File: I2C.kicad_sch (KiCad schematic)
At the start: 10 parts, among them J601 XH-4A connector, J602 2350514-8, U601 TLA2528IRTER

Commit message: update schematique
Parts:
- renumbered C601 to C26, C602 to C27, C603 to C28, J601 to J13, J602 to J14, R606 to R37, R607 to R38, R601 to R39, R602 to R40, U601 to U11
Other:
- title: 5V Logic I2C -> I2C
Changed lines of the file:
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@@
 	(paper "USLetter")
 	(title_block
-		(title "5V Logic I2C")
+		(title "I2C")
 		(comment 1 "Gérémy Sauvageau")
 	)
@@
 		(on_board yes)
 		(dnp no)
-		(property "Reference" "#PWR0615"
+		(property "Reference" "#PWR089"
 			(at 82.55 130.048 0)
 			(effects
@@
 			(project "SACE-HW"
 				(path "/4c1e5ca8-aa0f-4a8e-bffe-6765adb2e3e8/89fdb234-fe30-4f1f-ac7b-866137add73a"
-					(reference "#PWR0615")
+					(reference "#PWR089")
 					(unit 1)
 				)
@@
 		(dnp no)
 		(fields_autoplaced yes)
-		(property "Reference" "#PWR0605"
+		(property "Reference" "#PWR086"
 			(at 78.74 46.99 0)
 			(effects
@@
 			(project "SACE-HW"
 				(path "/4c1e5ca8-aa0f-4a8e-bffe-6765adb2e3e8/89fdb234-fe30-4f1f-ac7b-866137add73a"
-					(reference "#PWR0605")
+					(reference "#PWR086")
 					(unit 1)
 				)
@@
 		(dnp no)
 		(fields_autoplaced yes)
-		(property "Reference" "#PWR0601"
+		(property "Reference" "#PWR090"
 			(at 110.49 45.72 0)
 			(effects
@@
 			(project "SACE-HW"
 				(path "/4c1e5ca8-aa0f-4a8e-bffe-6765adb2e3e8/89fdb234-fe30-4f1f-ac7b-866137add73a"
-					(reference "#PWR0601")
+					(reference "#PWR090")
 					(unit 1)
 				)
@@
 		(dnp no)
 		(fields_autoplaced yes)
-		(property "Reference" "#PWR0603"
+		(property "Reference" "#PWR082"
 			(at 41.91 46.99 0)
 			(effects
@@
 			(project "SACE-HW"
 				(path "/4c1e5ca8-aa0f-4a8e-bffe-6765adb2e3e8/89fdb234-fe30-4f1f-ac7b-866137add73a"
-					(reference "#PWR0603")
+					(reference "#PWR082")
 					(unit 1)
 				)
@@
 		(on_board yes)
 		(dnp no)
-		(property "Reference" "#PWR0607"
+		(property "Reference" "#PWR087"
 			(at 78.74 58.928 0)
 			(effects
@@
 			(project "SACE-HW"
 				(path "/4c1e5ca8-aa0f-4a8e-bffe-6765adb2e3e8/89fdb234-fe30-4f1f-ac7b-866137add73a"
-					(reference "#PWR0607")
+					(reference "#PWR087")
 					(unit 1)
 				)
@@
 		(on_board yes)
 		(dnp no)
-		(property "Reference" "#PWR0606"
+		(property "Reference" "#PWR083"
 			(at 46.99 57.658 0)
 			(effects
@@
 			(project "SACE-HW"
 				(path "/4c1e5ca8-aa0f-4a8e-bffe-6765adb2e3e8/89fdb234-fe30-4f1f-ac7b-866137add73a"
-					(reference "#PWR0606")
+					(reference "#PWR083")
 					(unit 1)
 				)
@@
 		(on_board yes)
 		(dnp no)
-		(property "Reference" "U601"
+		(property "Reference" "U11"
 			(at 102.87 74.93 0)
 			(effects
@@
 			(project "SACE-HW"
 				(path "/4c1e5ca8-aa0f-4a8e-bffe-6765adb2e3e8/89fdb234-fe30-4f1f-ac7b-866137add73a"
-					(reference "U601")
+					(reference "U11")
 					(unit 1)
 				)
@@
 		(dnp no)
 		(fields_autoplaced yes)
-		(property "Reference" "#PWR0608"
+		(property "Reference" "#PWR088"
 			(at 81.28 86.36 0)
 			(effects
@@
 			(project "SACE-HW"
 				(path "/4c1e5ca8-aa0f-4a8e-bffe-6765adb2e3e8/89fdb234-fe30-4f1f-ac7b-866137add73a"
-					(reference "#PWR0608")
+					(reference "#PWR088")
 					(unit 1)
 				)
@@
 		(dnp no)
 		(fields_autoplaced yes)
-		(property "Reference" "R601"
+		(property "Reference" "R39"
 			(at 107.95 46.9899 90)
 			(effects
@@
 			(project "SACE-HW"
 				(path "/4c1e5ca8-aa0f-4a8e-bffe-6765adb2e3e8/89fdb234-fe30-4f1f-ac7b-866137add73a"
-					(reference "R601")
+					(reference "R39")
 					(unit 1)
 				)
@@
 		(on_board yes)
 		(dnp no)
-		(property "Reference" "#PWR0613"
+		(property "Reference" "#PWR085"
 			(at 69.85 118.618 0)
 			(effects
@@
 			(project "SACE-HW"
 				(path "/4c1e5ca8-aa0f-4a8e-bffe-6765adb2e3e8/89fdb234-fe30-4f1f-ac7b-866137add73a"
-					(reference "#PWR0613")
+					(reference "#PWR085")
 					(unit 1)
 				)
@@
 		(dnp no)
 		(fields_autoplaced yes)
-		(property "Reference" "#PWR0604"
+		(property "Reference" "#PWR084"
 			(at 52.07 46.99 0)
 			(effects
@@
 			(project "SACE-HW"
 				(path "/4c1e5ca8-aa0f-4a8e-bffe-6765adb2e3e8/89fdb234-fe30-4f1f-ac7b-866137add73a"
-					(reference "#PWR0604")
+					(reference "#PWR084")
 					(unit 1)
 				)
@@
 		(dnp no)
 		(fields_autoplaced yes)
-		(property "Reference" "J602"
+		(property "Reference" "J14"
 			(at 147.32 110.4899 0)
 			(effects
@@
 			(project "SACE-HW"
 				(path "/4c1e5ca8-aa0f-4a8e-bffe-6765adb2e3e8/89fdb234-fe30-4f1f-ac7b-866137add73a"
-					(reference "J602")
+					(reference "J14")
 					(unit 1)
 				)
@@
 		(dnp no)
 		(fields_autoplaced yes)
-		(property "Reference" "J601"
+		(property "Reference" "J13"
 			(at 71.755 40.64 0)
 			(effects
@@
 			(project "SACE-HW"
 				(path "/4c1e5ca8-aa0f-4a8e-bffe-6765adb2e3e8/89fdb234-fe30-4f1f-ac7b-866137add73a"
-					(reference "J601")
+					(reference "J13")
 					(unit 1)
 				)
@@
 		(dnp no)
 		(fields_autoplaced yes)
-		(property "Reference" "R602"
+		(property "Reference" "R40"
 			(at 118.11 46.9899 90)
 			(effects
@@
 			(project "SACE-HW"
 				(path "/4c1e5ca8-aa0f-4a8e-bffe-6765adb2e3e8/89fdb234-fe30-4f1f-ac7b-866137add73a"
-					(reference "R602")
+					(reference "R40")
 					(unit 1)
 				)
@@
 		(on_board yes)
 		(dnp no)
-		(property "Reference" "C602"
+		(property "Reference" "C27"
 			(at 52.07 44.45 90)
 			(effects
@@
 			(project "SACE-HW"
 				(path "/4c1e5ca8-aa0f-4a8e-bffe-6765adb2e3e8/89fdb234-fe30-4f1f-ac7b-866137add73a"
-					(reference "C602")
+					(reference "C27")
 					(unit 1)
 				)
@@
 		(on_board yes)
 		(dnp no)
-		(property "Reference" "C601"
+		(property "Reference" "C26"
 			(at 41.91 44.45 90)
 			(effects
@@
 			(project "SACE-HW"
 				(path "/4c1e5ca8-aa0f-4a8e-bffe-6765adb2e3e8/89fdb234-fe30-4f1f-ac7b-866137add73a"
-					(reference "C601")
+					(reference "C26")
 					(unit 1)
 				)
@@
 		(on_board yes)
 		(dnp no)
-		(property "Reference" "R606"
+		(property "Reference" "R37"
 			(at 68.58 95.25 90)
 			(effects
@@
 			(project "SACE-HW"
 				(path "/4c1e5ca8-aa0f-4a8e-bffe-6765adb2e3e8/89fdb234-fe30-4f1f-ac7b-866137add73a"
-					(reference "R606")
+					(reference "R37")
 					(unit 1)
 				)
@@
 		(on_board yes)
 		(dnp yes)
-		(property "Reference" "R607"
+		(property "Reference" "R38"
 			(at 68.58 105.41 90)
 			(effects
@@
 			(project "SACE-HW"
 				(path "/4c1e5ca8-aa0f-4a8e-bffe-6765adb2e3e8/89fdb234-fe30-4f1f-ac7b-866137add73a"
-					(reference "R607")
+					(reference "R38")
 					(unit 1)
 				)
@@
 		(on_board yes)
 		(dnp no)
-		(property "Reference" "#PWR0610"
+		(property "Reference" "#PWR091"
 			(at 123.19 89.408 0)
 			(effects
@@
 			(project "SACE-HW"
 				(path "/4c1e5ca8-aa0f-4a8e-bffe-6765adb2e3e8/89fdb234-fe30-4f1f-ac7b-866137add73a"
-					(reference "#PWR0610")
+					(reference "#PWR091")
 					(unit 1)
 				)
@@
 		(on_board yes)
 		(dnp no)
-		(property "Reference" "C603"
+		(property "Reference" "C28"
 			(at 81.28 120.65 90)
 			(effects
@@
 			(project "SACE-HW"
 				(path "/4c1e5ca8-aa0f-4a8e-bffe-6765adb2e3e8/89fdb234-fe30-4f1f-ac7b-866137add73a"
-					(reference "C603")
+					(reference "C28")
 					(unit 1)
 				)

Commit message: update schematique
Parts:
- added C603, C604, C606, C607, C608: 885012107015, Capacitors:C0603, symbol Capacitors:885012106022
- added J602: XH-4A connector, Connectors:XH-4A, symbol Connectors:XH-4A connector
- added J603, J605: 2350514-8, Connectors:CONN8_2350514-8_TEC, symbol Connectors:2350514-8
- added R605, R609: RC0805JR-072K2L, Resistors:R0805, symbol Resistors:RC0805JR-072K2L
- added R606, R607, R611, R612: RC0805JR-0710KL, Resistors:R0805, symbol Resistors:RC0805JR-0710KL
- added R608: RC0805JR-07100KL, Resistors:R0805, symbol Resistors:RC0805JR-07100KL
- added R610: RC0805JR-070RL, Resistors:R0603, symbol Resistors:RC0805JR-070RL
- added U601: MCP4728T-E_UN, IC:SOP50P490X110-10N, symbol DAC:MCP4728T-E_UN
- added U603: TLV9302IDR, Assembly:IC8_TLV9302IDR_TEX, symbol Amplifiers:TLV9302IDR
- added U604: TLA2528IRTER, QFN50P300X300X80-17N-D, symbol ADC:TLA2528IRTER
- renumbered C26 to C601, C27 to C602, C28 to C605, J13 to J601, J14 to J604, R39 to R601, R40 to R602, R37 to R603, R38 to R604, U11 to U602
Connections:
- net 5VB: now also C603.2, C604.2, C606.2, C607.2, J602.4, U601.1 (VDD), U604.10 (DVDD), U604.7 (AVDD)
- net GNDB: now also C603.1, C604.1, C606.1, C607.1, C608.1, J602.1, J603.5, J603.6, J603.7, J603.8, R605.1, R606.1, R609.1, R610.2, R611.1, U601.10 (VSS), U603.4, U604.17 (EP), U604.9 (GND)
- net SCL: now also J602.3, U601.2 (SCL), U604.13 (SCL)
- net SDA: now also J602.2, U601.3 (SDA), U604.14 (SDA)
- net decap: now also C608.2, R608.1, U604.8 (DECAP)
- new net: R611.2, R612.1, U603.6
- new net: R608.2, R610.1, U604.11 (ADDR)
- new net: R606.2, R607.1, U603.2
- new net: J605.1, U604.15 (AIN0/GPIO0)
- new net: J605.2, U604.16 (AIN1/GPIO1)
- new net: J605.3, U604.1 (AIN2/GPIO2)
- new net: J605.4, U604.2 (AIN3/GPIO3)
- new net: J605.5, U604.3 (AIN4/GPIO4)
- new net: J605.6, U604.4 (AIN5/GPIO5)
- new net: J605.7, U604.5 (AIN6/GPIO6)
- new net: J605.8, U604.6 (AIN7/GPIO7)
- new net 12VB: U603.8
- new net OUTA: U601.6 (VOUTA), U603.3
- new net OUTA_10V: J603.1
- new net OUTA_12V: R605.2, R607.2, R609.2, R612.2, U603.1, U603.7
- new net OUTB: U601.7 (VOUTB), U603.5
- new net OUTB_10V: J603.2
- new net OUTC: J603.3, U601.8 (VOUTC)
- new net OUTD: J603.4, U601.9 (VOUTD)
- no-connect marks 0 -> 2
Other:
- note added: "Current addr: 0x14 (Check P.15 datasheet)"
- note added: "DEFAULT ADDR: 0x00"
- moved on the sheet: C601, C602, C605, J601, J604, R601, R602, R603, R604, U602

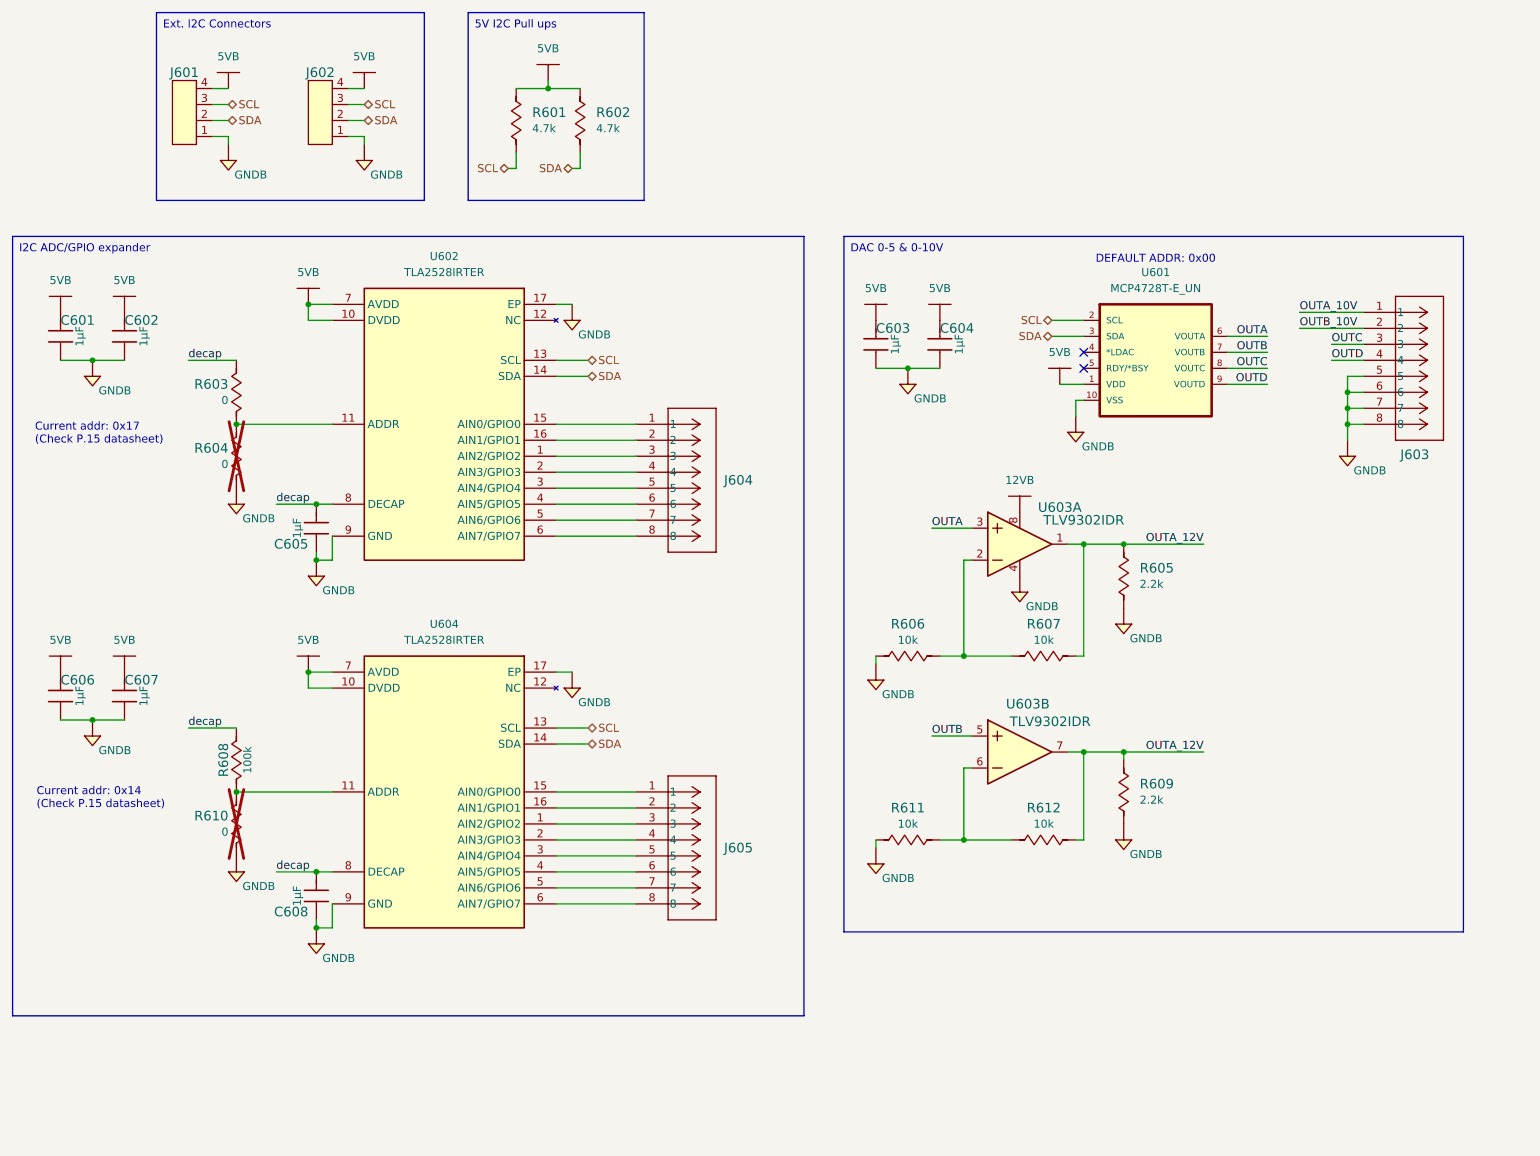
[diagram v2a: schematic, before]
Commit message: update schematic
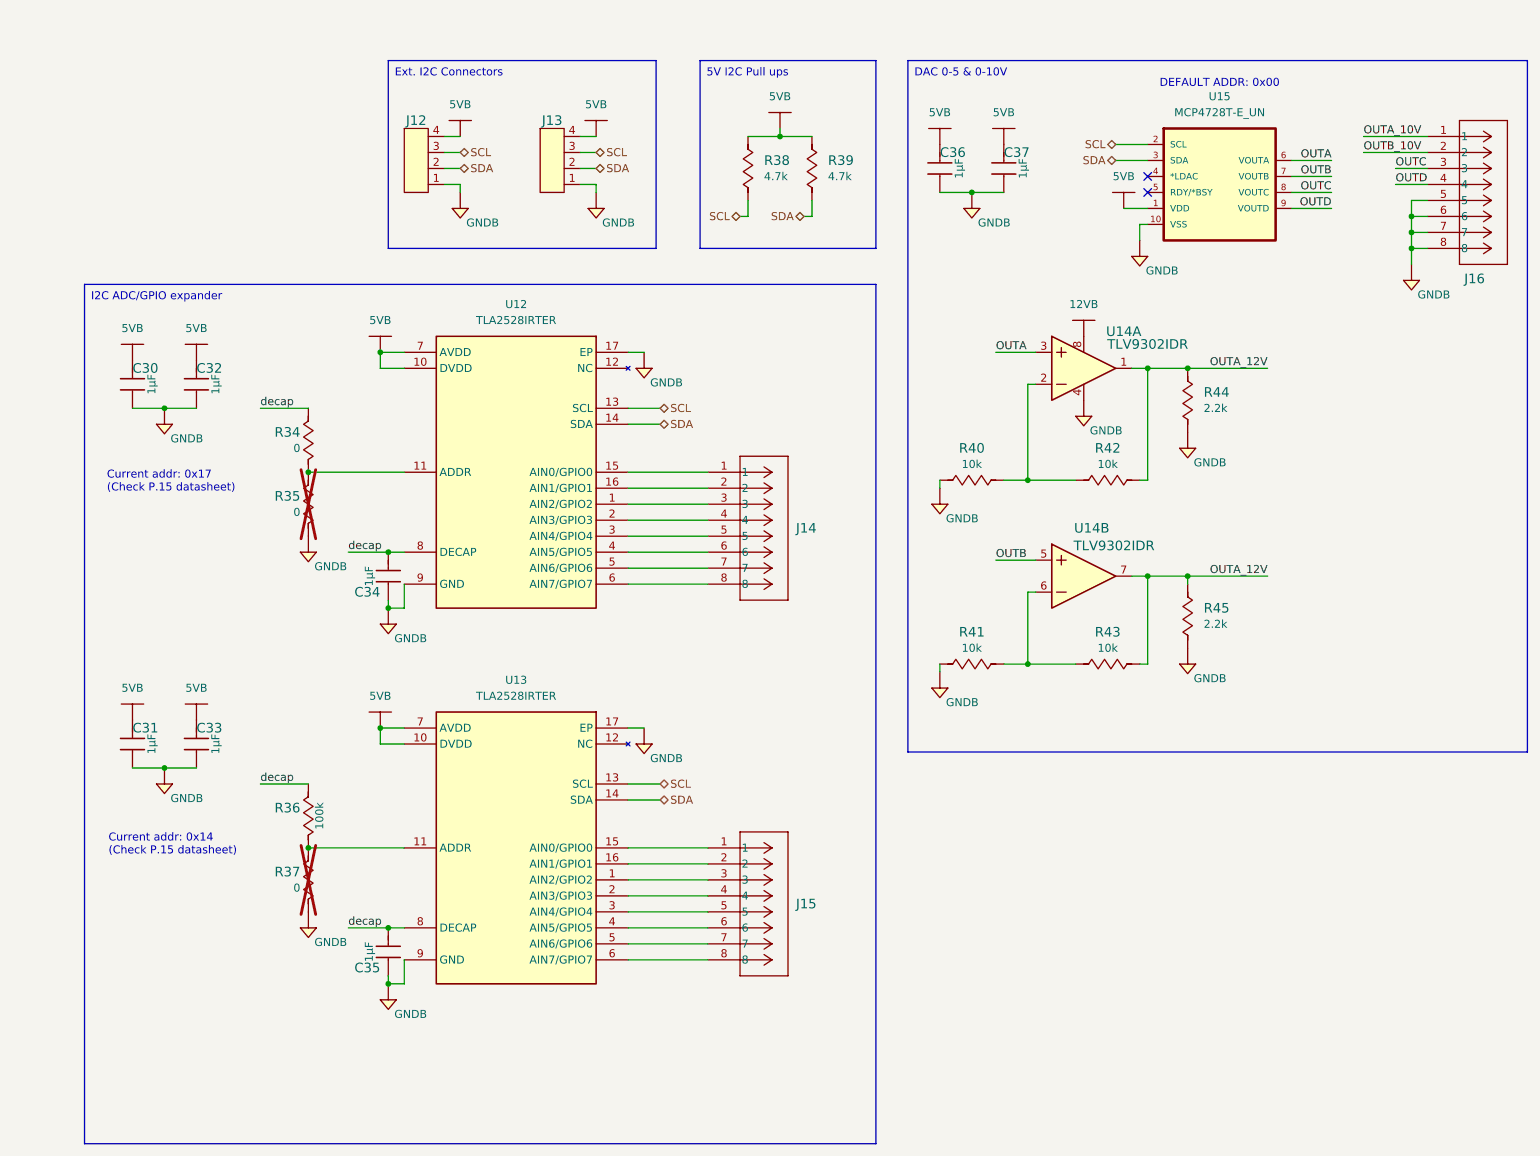
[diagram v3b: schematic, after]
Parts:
- removed C606, C607, C608: 885012107015, Capacitors:C0603, symbol Capacitors:885012106022
- removed J605: 2350514-8, Connectors:CONN8_2350514-8_TEC, symbol Connectors:2350514-8
- removed R608: RC0805JR-07100KL, Resistors:R0805, symbol Resistors:RC0805JR-07100KL
- removed R610: RC0805JR-070RL, Resistors:R0603, symbol Resistors:RC0805JR-070RL
- removed U604: TLA2528IRTER, QFN50P300X300X80-17N-D, symbol ADC:TLA2528IRTER
- added C31, C33, C35: 885012107015, Capacitors:C0603, symbol Capacitors:885012106022
- added J15: 2350514-8, Connectors:CONN8_2350514-8_TEC, symbol Connectors:2350514-8
- added R36: RC0805JR-070RL, Resistors:R0805, symbol Resistors:RC0805JR-07100KL
- added R37: RC0805JR-070RL, Resistors:R0603, symbol Resistors:RC0805JR-070RL
- added U13: TLA2528IRTER, QFN50P300X300X80-17N-D, symbol ADC:TLA2528IRTER
- renumbered C601 to C30, C602 to C32, C605 to C34, C603 to C36, C604 to C37, J601 to J12, J602 to J13, J604 to J14, J603 to J16, R603 to R34, R604 to R35, R601 to R38, R602 to R39, R606 to R40, R611 to R41, R607 to R42, R612 to R43, R605 to R44, R609 to R45, U602 to U12, U603 to U14, U601 to U15
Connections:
- net 5VB: now also C31.2, C33.2, U13.10 (DVDD), U13.7 (AVDD)
- net GNDB: now also C31.1, C33.1, C35.1, R37.2, U13.17 (EP), U13.9 (GND)
- net SCL: now also U13.13 (SCL)
- net SDA: now also U13.14 (SDA)
- net decap: now also C35.2, R36.1, U13.8 (DECAP)
- new net: J15.1, U13.15 (AIN0/GPIO0)
- new net: J15.2, U13.16 (AIN1/GPIO1)
- new net: J15.3, U13.1 (AIN2/GPIO2)
- new net: J15.4, U13.2 (AIN3/GPIO3)
- new net: J15.5, U13.3 (AIN4/GPIO4)
- new net: J15.6, U13.4 (AIN5/GPIO5)
- new net: J15.7, U13.5 (AIN6/GPIO6)
- new net: J15.8, U13.6 (AIN7/GPIO7)
- new net: R36.2, R37.1, U13.11 (ADDR)
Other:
- moved on the sheet: C30, C32, C34, C36, C37, J12, J13, J14, J16, R34, R35, R38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

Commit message: finalisation de la schématique
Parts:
- renumbered C36 to C601, C37 to C602, C30 to C603, C32 to C604, C34 to C605, C31 to C606, C33 to C607, C35 to C608, J16 to J601, J12 to J602, J13 to J603, J14 to J604, J15 to J605, R38 to R601, R39 to R602, R44 to R603, R34 to R604, R40 to R605, R42 to R606, R35 to R607, R45 to R608, R41 to R609, R43 to R610, R36 to R611, R37 to R612, U15 to U601, U14 to U602, U12 to U603, U13 to U604
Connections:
- net OUTA_10V: now also R603.2, R606.2, U602.1
- net OUTB_10V: now also R608.2, R610.2, U602.7
- removed net OUTA_12V: R603.2, R606.2, R608.2, R610.2, U602.1, U602.7
